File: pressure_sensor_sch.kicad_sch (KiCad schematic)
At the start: 37 parts, among them J13 1053131104, U9 ADS131M06IRSNR

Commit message: Completed schematics
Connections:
- net +10V renamed +12V
- no-connect marks 2 -> 8
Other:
- note added: "Voltage drawn across R34, R39, and R44 to be 1.2v max to match ADS input range"

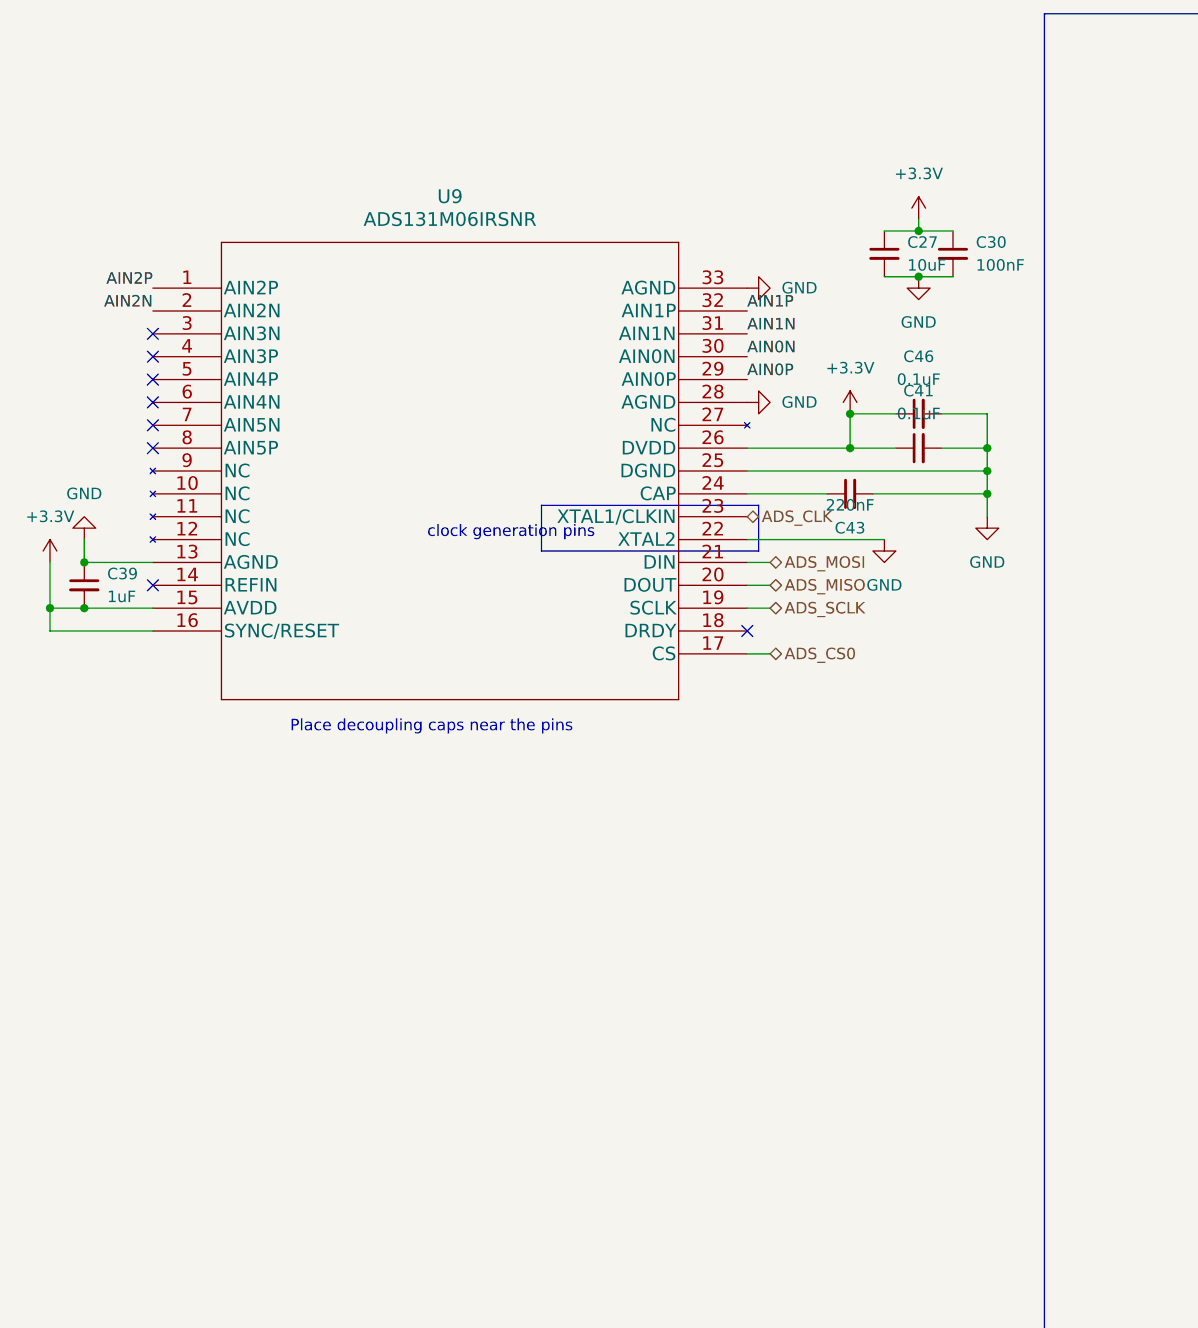
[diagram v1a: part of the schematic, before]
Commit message: Xavier: Modified ADS board
Pressure Sensor ADS board reduced to ADS131M03 with 3 channels for the 3 pressure sensors
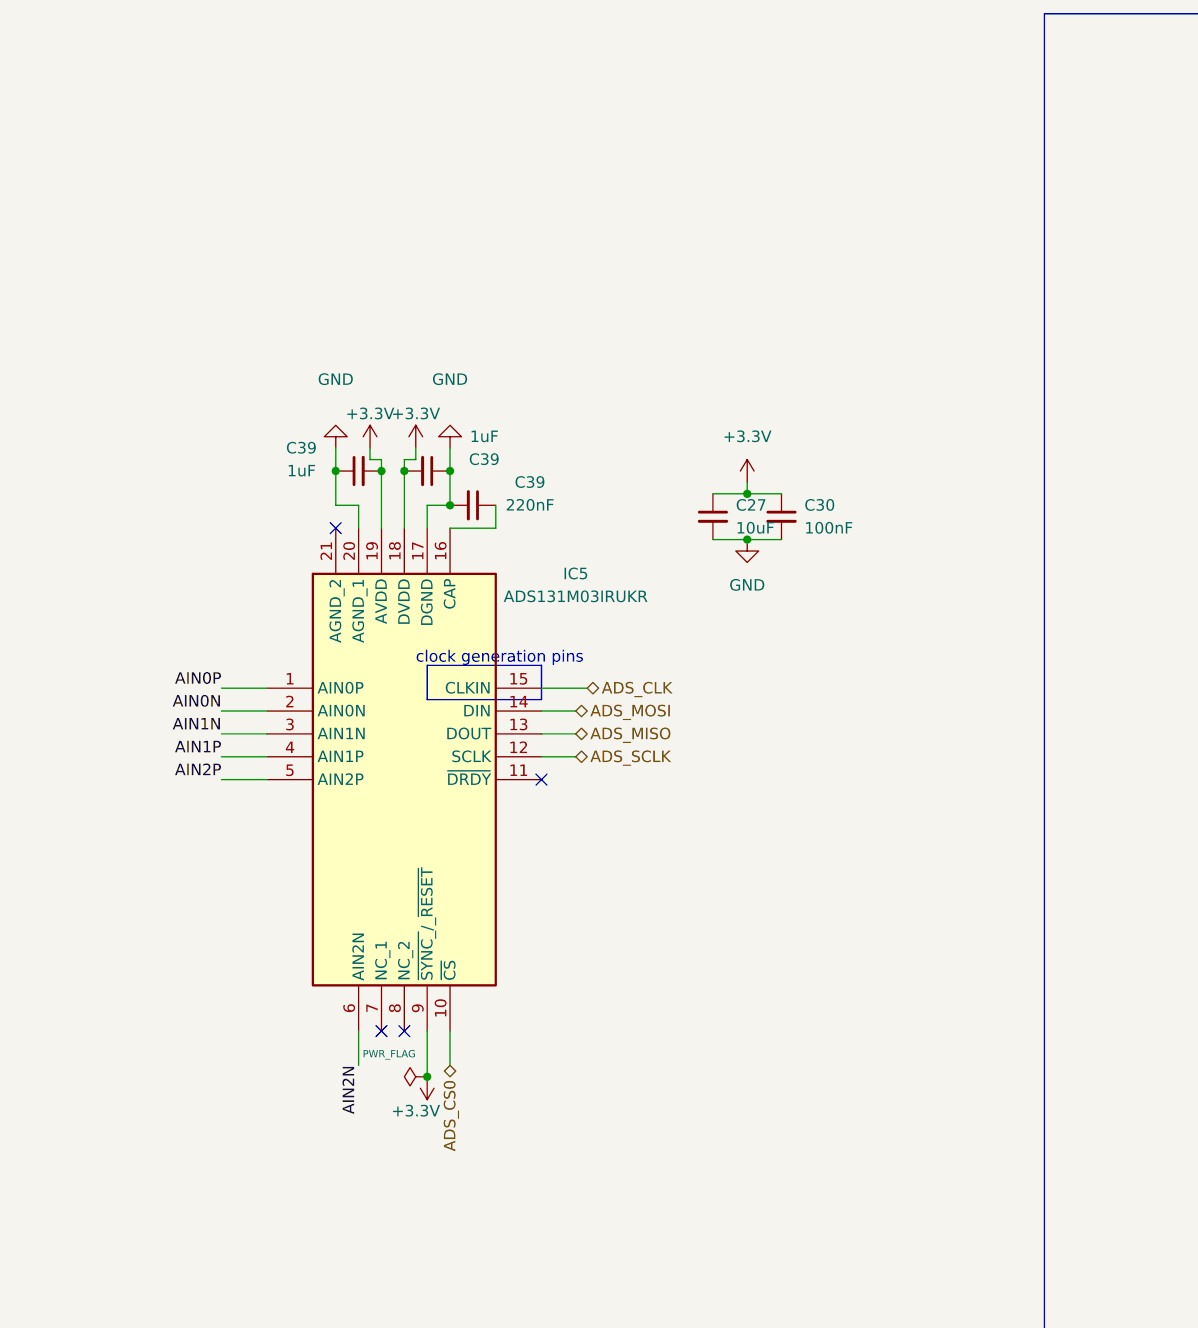
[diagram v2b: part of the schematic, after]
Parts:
- removed C39: 1uF, Capacitor_SMD:C_0402_1005Metric, symbol Device:C_Small
- removed C41, C46: 0.1uF, Capacitor_SMD:C_0402_1005Metric, symbol Device:C_Small
- removed C43: 220nF, Capacitor_SMD:C_0402_1005Metric, symbol Device:C_Small
- removed U9: ADS131M06IRSNR, iclr:ADS131M06IRSNR, symbol iclr:ADS131M06IRSNR
- added C39 (x2): 1uF, Capacitor_SMD:C_0402_1005Metric, symbol Device:C_Small
- added C39: 220nF, Capacitor_SMD:C_0402_1005Metric, symbol Device:C_Small
- added IC5: ADS131M03IRUKR, QFN40P300X300X80-21N-D, symbol SamacSys_Parts:ADS131M03IRUKR
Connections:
- net +3V3: now also C39.2, C39.2, IC5.18 (DVDD), IC5.19 (AVDD)
- net ADS_CLK: now also IC5.15 (CLKIN)
- net ADS_CS0: now also IC5.10 (~{CS})
- net ADS_MISO: now also IC5.13 (DOUT)
- net ADS_MOSI: now also IC5.14 (DIN)
- net ADS_SCLK: now also IC5.12 (SCLK)
- net AIN0N: now also IC5.2 (AIN0N)
- net AIN0P: now also IC5.1 (AIN0P)
- net AIN1N: now also IC5.3 (AIN1N)
- net AIN1P: now also IC5.4 (AIN1P)
- net AIN2N: now also IC5.6 (AIN2N)
- net AIN2P: now also IC5.5 (AIN2P)
- net GND: now also C39.1, C39.1, C39.2, IC5.17 (DGND), IC5.20 (AGND_1)
- new net: C39.1, IC5.16 (CAP)
- new net +3.3V: IC5.9 (~{SYNC_}/_~{RESET})
- no-connect marks 8 -> 4
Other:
- note removed: "Place decoupling caps near the pins"

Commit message: Finished schematic
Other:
- moved on the sheet: J13, JP31, JP35, JP39, R61

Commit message: update
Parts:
- removed C39 (x2): 1uF, Capacitor_SMD:C_0402_1005Metric, symbol Device:C_Small
- removed C39: 220nF, Capacitor_SMD:C_0402_1005Metric, symbol Device:C_Small
- removed IC5: ADS131M03IRUKR, QFN40P300X300X80-21N-D, symbol SamacSys_Parts:ADS131M03IRUKR
- removed R61: 113k, Resistor_SMD:R_0402_1005Metric, symbol Device:R_Small
- removed R61: 40.2k, Resistor_SMD:R_0402_1005Metric, symbol Device:R_Small
- removed R61: 1k, Resistor_SMD:R_0402_1005Metric, symbol Device:R_Small
- added C39 (x2): 1uF, Capacitor_SMD:C_0402_1005Metric, symbol Device:C_Small
- added C73 (x3): 10nF, Capacitor_SMD:C_0402_1005Metric, symbol Device:C_Small
- added J13 (x3): 1053131104, Connector_Molex:Molex_Nano-Fit_105313-xx04_1x04_P2.50mm_Horizontal, symbol iclr:1053131104
- added JP31 (x3): SolderJumper_2_Open, Jumper:SolderJumper-2_P1.3mm_Open_RoundedPad1.0x1.5mm, symbol Jumper:SolderJumper_2_Open
- added JP35 (x3), JP39 (x3): SolderJumper_3_Open, Jumper:SolderJumper-3_P1.3mm_Open_RoundedPad1.0x1.5mm_NumberLabels, symbol Jumper:SolderJumper_3_Open
- added R61 (x3): 40.2k, Resistor_SMD:R_0402_1005Metric, symbol Device:R_Small
- added R61 (x3): 49k, Resistor_SMD:R_0402_1005Metric, symbol Device:R_Small
- added R61 (x6): 1k, Resistor_SMD:R_0402_1005Metric, symbol Device:R_Small
- added R61: 10k, Resistor_SMD:R_0402_1005Metric, symbol Device:R_Small
- added R61 (x3): 113k, Resistor_SMD:R_0402_1005Metric, symbol Device:R_Small
- added R61: 76k, Resistor_SMD:R_0402_1005Metric, symbol Device:R_Small
- added U8: ADS131M06IPBS, iclr:ADS131M06IRSNR, symbol 2024-03-09_17-28-43:ADS131M06IPBS
- J13: footprint iclr:1053131104 -> Connector_Molex:Molex_Nano-Fit_105313-xx04_1x04_P2.50mm_Horizontal
- R61: value 49k -> 10k
- R61: value 1k -> 14k
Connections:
- net +12V: now also JP35.3 (B), JP35.3 (B), JP35.3 (B)
- net +3.3V: now also U8.16 (SYNC/RESET)
- net +3V3: now also C39.1, C39.2, U8.15 (AVDD), U8.26 (DVDD)
- net +5V: now also JP35.1 (A), JP35.1 (A), JP35.1 (A)
- net ADS_CLK: now also U8.23 (XTAL1/CLKIN)
- net ADS_CS0: now also U8.17 (CS)
- net ADS_MISO: now also U8.20 (DOUT)
- net ADS_MOSI: now also U8.21 (DIN)
- net ADS_SCLK: now also U8.19 (SCLK)
- net AIN0N: now also U8.30 (AIM0N)
- net AIN0P: now also R61.2, U8.29 (AIN0P); no longer JP39.3 (B)
- net AIN1N: now also U8.31 (AIN1N)
- net AIN1P: now also U8.32 (AIN1P)
- net AIN2N: now also U8.2 (AIN2N)
- net AIN2P: now also U8.1 (AIN2P)
- net GND: now also C39.1, C39.2, J13.4, J13.4, J13.4, JP31.1 (A), JP31.1 (A), JP31.1 (A), U8.13 (AGND), U8.25 (DGND)
- net at R61.1: now also JP39.1 (A)
- net at J13.2: now also R61.2; no longer JP39.2 (C)
- new net: R61.1, R61.2 (x6)
- new net: J13.1, JP35.2 (C) (x3)
- new net: JP39.1 (A), R61.2 (x3)
- new net: J13.2, JP39.2 (C) (x3)
- new net: JP39.3 (B), R61.1
- new net: R61.1, R61.1 (x3)
- new net: JP39.2 (C), R61.1
- new net AIN3N: C73.2, J13.3, JP31.2 (B), R61.2, U8.3 (AIN3N)
- new net AIN3P: C73.1, JP39.3 (B), R61.1, R61.2, U8.4 (AIN3P)
- new net AIN4N: C73.2, J13.3, JP31.2 (B), R61.2, U8.6 (AIN4N)
- new net AIN4P: C73.1, JP39.3 (B), R61.1, R61.2, U8.5 (AIN4P)
- new net AIN5N: C73.2, J13.3, JP31.2 (B), R61.2, U8.7 (AIN5N)
- new net AIN5P: C73.1, JP39.3 (B), R61.1, R61.2, U8.8 (AIN5P)
- no-connect marks 4 -> 1
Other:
- note removed: "clock generation pins"
- moved on the sheet: C27, C30, J13, JP31, JP35, JP39, R61

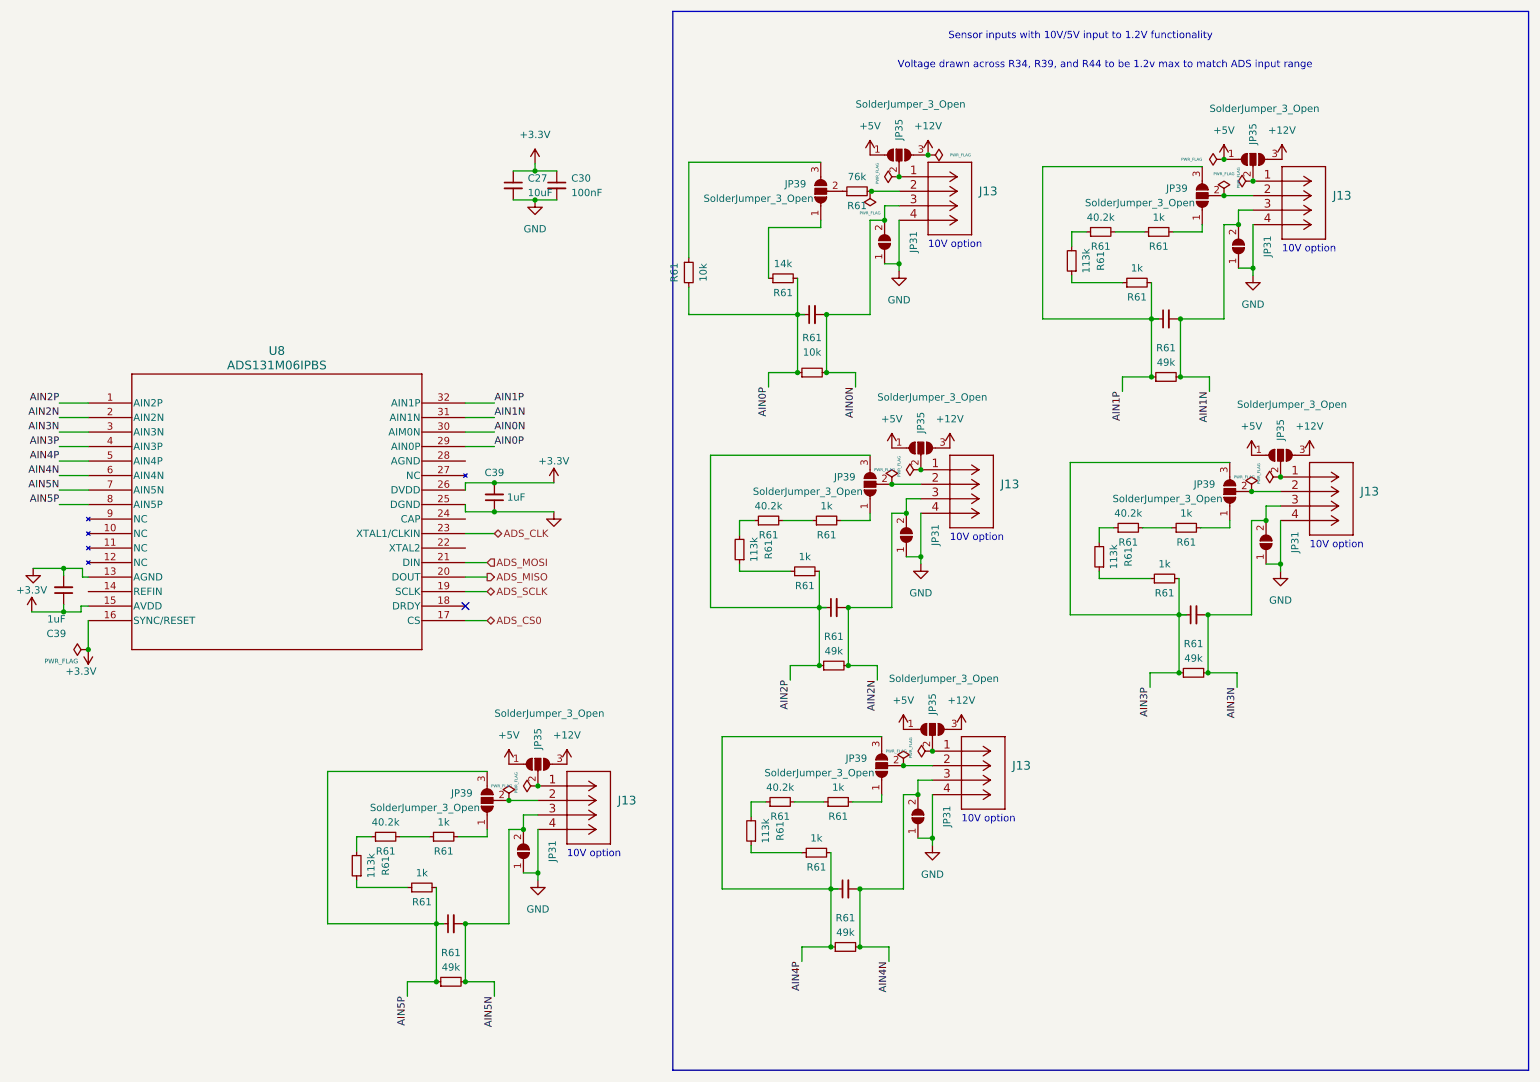
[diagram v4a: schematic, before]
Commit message: Schematic done, components layed out, sensors wired up
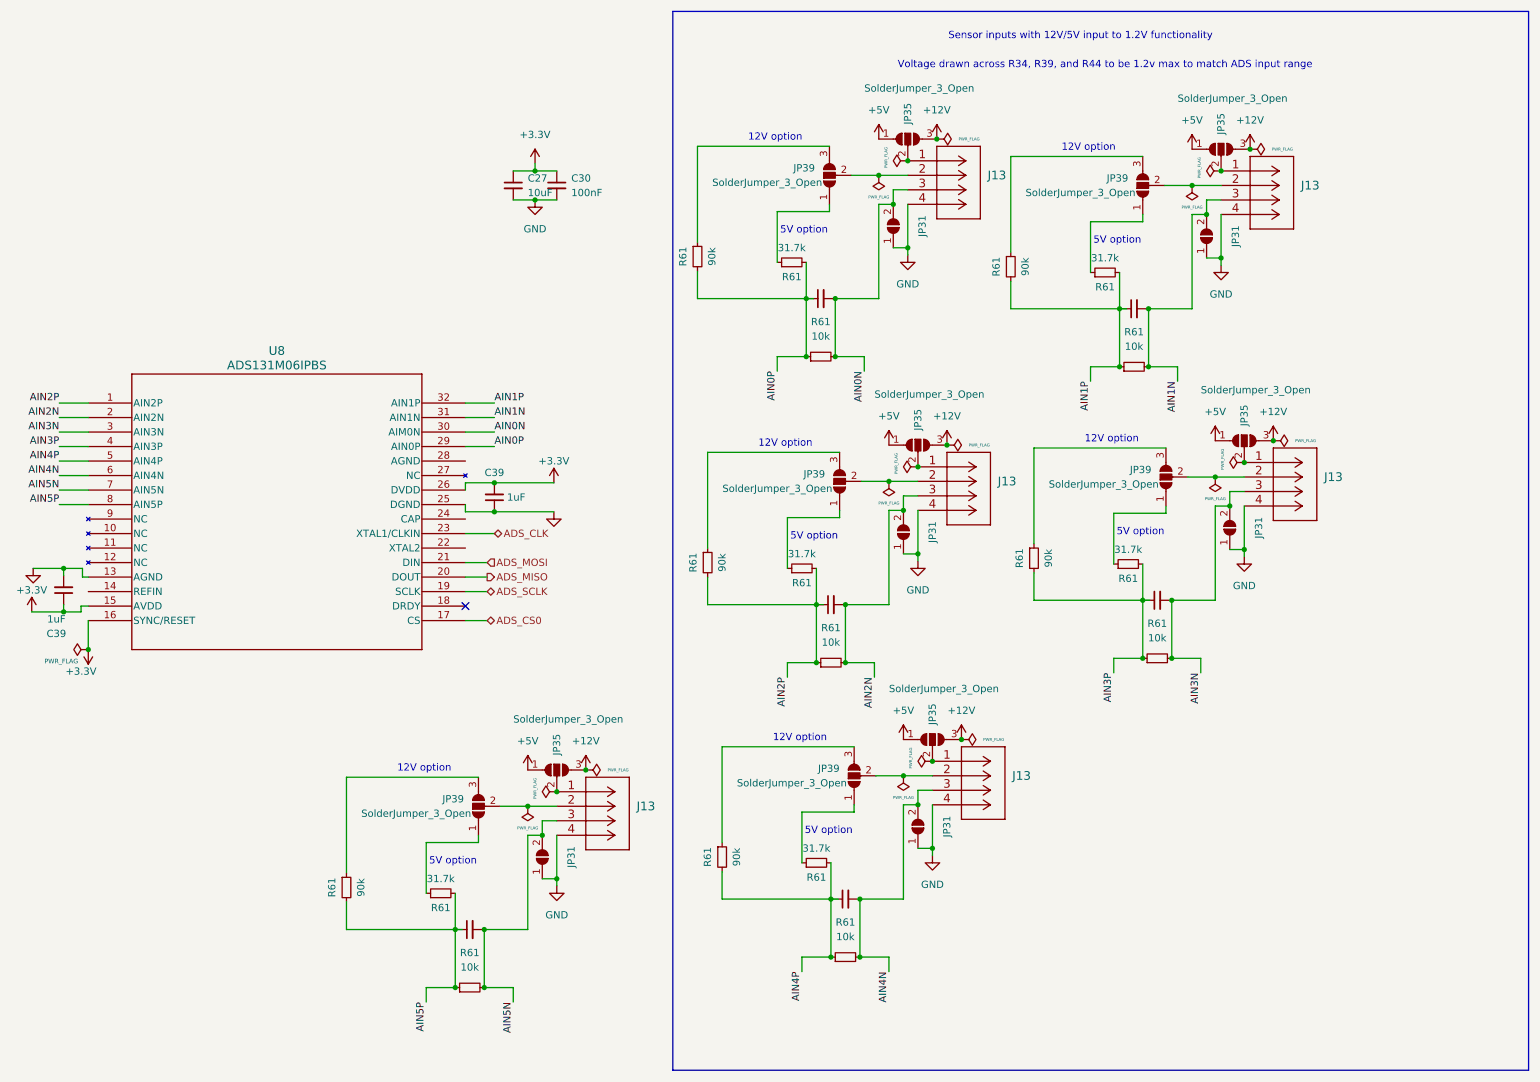
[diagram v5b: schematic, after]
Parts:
- removed C73 (x6): 10nF, Capacitor_SMD:C_0402_1005Metric, symbol Device:C_Small
- removed J13 (x6): 1053131104, Connector_Molex:Molex_Nano-Fit_105313-xx04_1x04_P2.50mm_Horizontal, symbol iclr:1053131104
- removed JP31 (x6): SolderJumper_2_Open, Jumper:SolderJumper-2_P1.3mm_Open_RoundedPad1.0x1.5mm, symbol Jumper:SolderJumper_2_Open
- removed JP35 (x6), JP39 (x6): SolderJumper_3_Open, Jumper:SolderJumper-3_P1.3mm_Open_RoundedPad1.0x1.5mm_NumberLabels, symbol Jumper:SolderJumper_3_Open
- removed R61 (x5): 40.2k, Resistor_SMD:R_0402_1005Metric, symbol Device:R_Small
- removed R61 (x2): 10k, Resistor_SMD:R_0402_1005Metric, symbol Device:R_Small
- removed R61 (x5): 49k, Resistor_SMD:R_0402_1005Metric, symbol Device:R_Small
- removed R61 (x10): 1k, Resistor_SMD:R_0402_1005Metric, symbol Device:R_Small
- removed R61 (x5): 113k, Resistor_SMD:R_0402_1005Metric, symbol Device:R_Small
- removed R61: 14k, Resistor_SMD:R_0402_1005Metric, symbol Device:R_Small
- removed R61: 76k, Resistor_SMD:R_0402_1005Metric, symbol Device:R_Small
- added C73 (x6): 10nF, Capacitor_SMD:C_0402_1005Metric, symbol Device:C_Small
- added J13 (x6): 1053131104, Connector_Molex:Molex_Nano-Fit_105313-xx04_1x04_P2.50mm_Horizontal, symbol iclr:1053131104
- added JP31 (x6): SolderJumper_2_Open, Jumper:SolderJumper-2_P1.3mm_Open_RoundedPad1.0x1.5mm, symbol Jumper:SolderJumper_2_Open
- added JP35 (x6), JP39 (x6): SolderJumper_3_Open, Jumper:SolderJumper-3_P1.3mm_Open_RoundedPad1.0x1.5mm_NumberLabels, symbol Jumper:SolderJumper_3_Open
- added R61 (x6): 31.7k, Resistor_SMD:R_0402_1005Metric, symbol Device:R_Small
- added R61 (x6): 90k, Resistor_SMD:R_0402_1005Metric, symbol Device:R_Small
- added R61 (x6): 10k, Resistor_SMD:R_0402_1005Metric, symbol Device:R_Small
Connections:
- net +12V: now also JP35.3 (B), JP35.3 (B), JP35.3 (B), JP35.3 (B), JP35.3 (B), JP35.3 (B)
- net +5V: now also JP35.1 (A), JP35.1 (A), JP35.1 (A), JP35.1 (A), JP35.1 (A), JP35.1 (A)
- net AIN0N: now also C73.2, J13.3, JP31.2 (B), R61.2
- net AIN0P: now also C73.1, R61.1, R61.2, R61.2
- net AIN1N: now also C73.2, J13.3, JP31.2 (B), R61.2
- net AIN1P: now also C73.1, R61.1, R61.2, R61.2
- net AIN2N: now also C73.2, J13.3, JP31.2 (B), R61.2
- net AIN2P: now also C73.1, R61.1, R61.2, R61.2
- net AIN3N: now also C73.2, J13.3, JP31.2 (B), R61.2
- net AIN3P: now also C73.1, R61.1, R61.2, R61.2
- net AIN4N: now also C73.2, J13.3, JP31.2 (B), R61.2
- net AIN4P: now also C73.1, R61.1, R61.2, R61.2
- net AIN5N: now also C73.2, J13.3, JP31.2 (B), R61.2
- net AIN5P: now also C73.1, R61.1, R61.2, R61.2
- net GND: now also J13.4, J13.4, J13.4, J13.4, J13.4, J13.4, JP31.1 (A), JP31.1 (A), JP31.1 (A), JP31.1 (A), JP31.1 (A), JP31.1 (A)
- new net: J13.1, JP35.2 (C) (x6)
- new net: J13.2, JP39.2 (C) (x6)
- new net: JP39.1 (A), R61.1 (x6)
- new net: JP39.3 (B), R61.1 (x6)
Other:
- note added: "12V option"
- note added: "5V option"
- note added: "Sensor inputs with 12V/5V input to 1.2V functionality"
- note removed: "10V option"
- note removed: "Sensor inputs with 10V/5V input to 1.2V functionality"

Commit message: Wired up more stuff
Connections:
- net +3V3 is gone; now on net +3.3V: C27.1, C30.1, C39.1, C39.2, U8.15 (AVDD), U8.26 (DVDD)
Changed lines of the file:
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@@
   (junction (at 157.988 62.992) (diameter 0) (color 0 0 0 0)
   )
+  (junction (at 32.258 116.84) (diameter 0) (color 0 0 0 0)
+  )
   (junction (at 110.49 45.72) (diameter 0) (color 0 0 0 0)
   )
@@
   )
   (junction (at 185.166 140.208) (diameter 0) (color 0 0 0 0)
+  )
+  (junction (at 32.258 119.38) (diameter 0) (color 0 0 0 0)
   )
   (junction (at 221.996 125.984) (diameter 0) (color 0 0 0 0)
@@
     (stroke (width 0) (type default))
   )
+  (wire (pts (xy 32.258 116.84) (xy 32.258 119.38))
+    (stroke (width 0) (type default))
+  )
